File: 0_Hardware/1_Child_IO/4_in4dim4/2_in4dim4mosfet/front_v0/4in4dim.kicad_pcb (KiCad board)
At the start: 2 copper layers, 100.1 x 86.4 mm, 37 parts, among them IC1 ATTINY48-A, P1 CONN_8X2, P2 CONN_2, P3 CONN_2, P4 CONN_2, P5 CONN_2, Q1 PNP, Q2 PNP, Q3 PNP, Q4 PNP

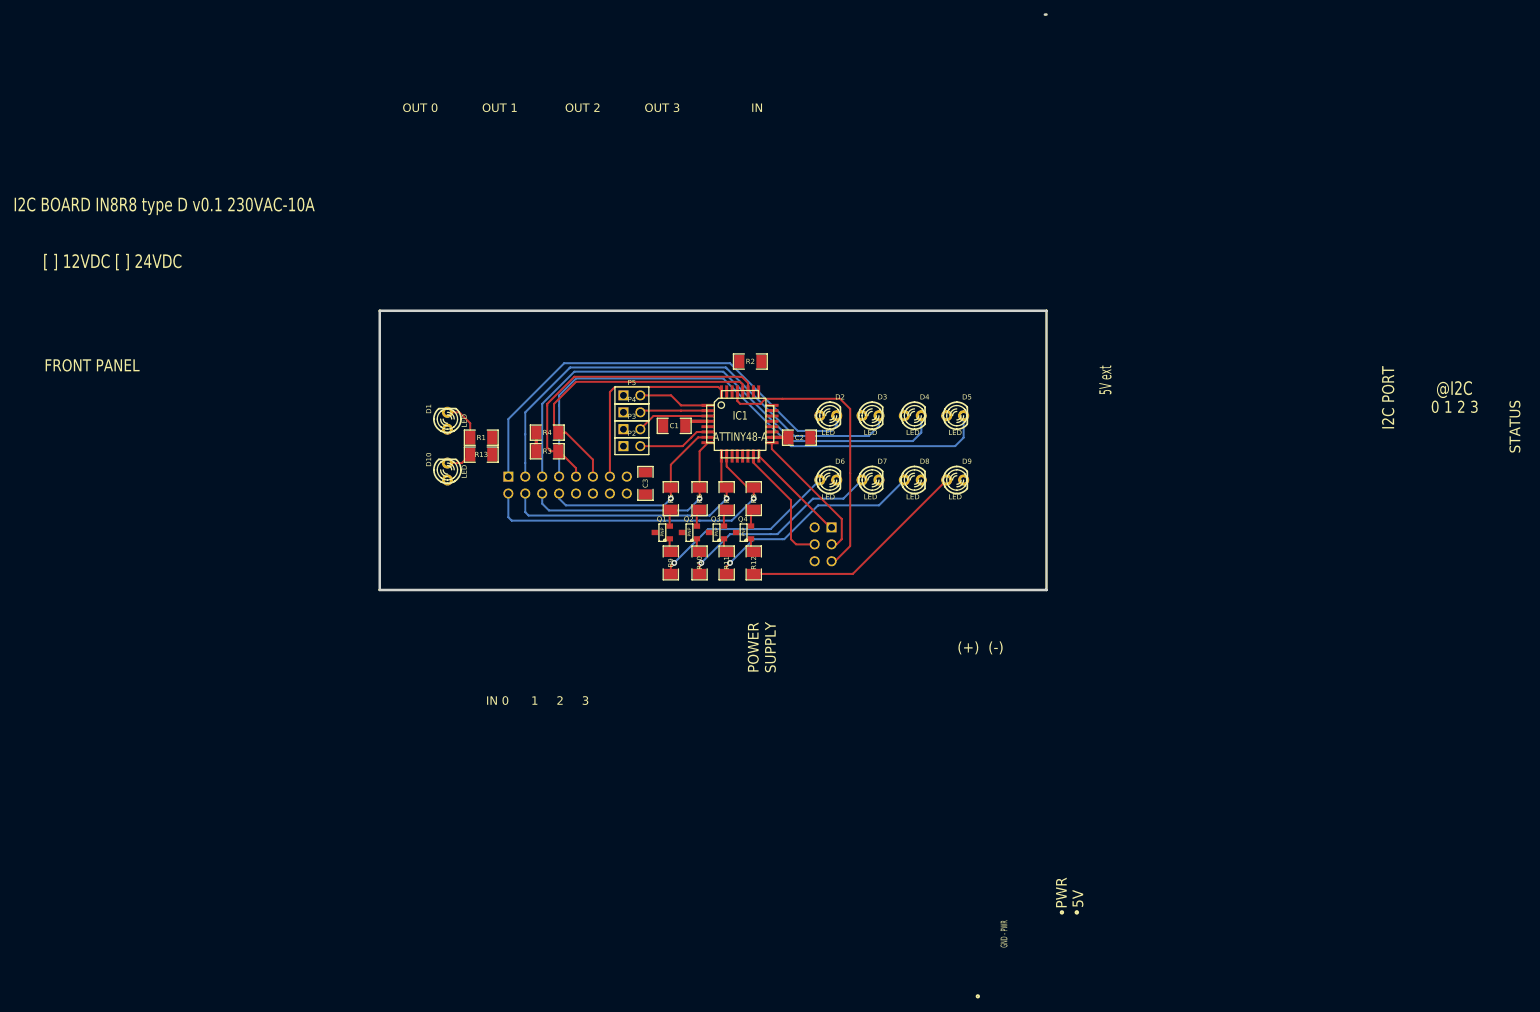
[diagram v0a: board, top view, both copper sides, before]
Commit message: Mise à jour du PCB Front Panel in4dim4mosfet   -> Inversion des broches dans le schéma pour faciliter le routage        * CMD0 Broche7 => Broche 10 de l'attiny        * CMD1 Broche8 => Broche 9 de l'attiny        * CMD2 Broche9 => Broche 8 de l'attiny        * CMD3 Broche10 => Broche 8 de l'attiny   -> Changement des types de led pour D2 à D9 (Transverse en CMS)   -> Mise en place des plan de masse des deux côtés
Mise à jour nom dans les gerber SMB V0.0 pour éviter les pb Smartgit
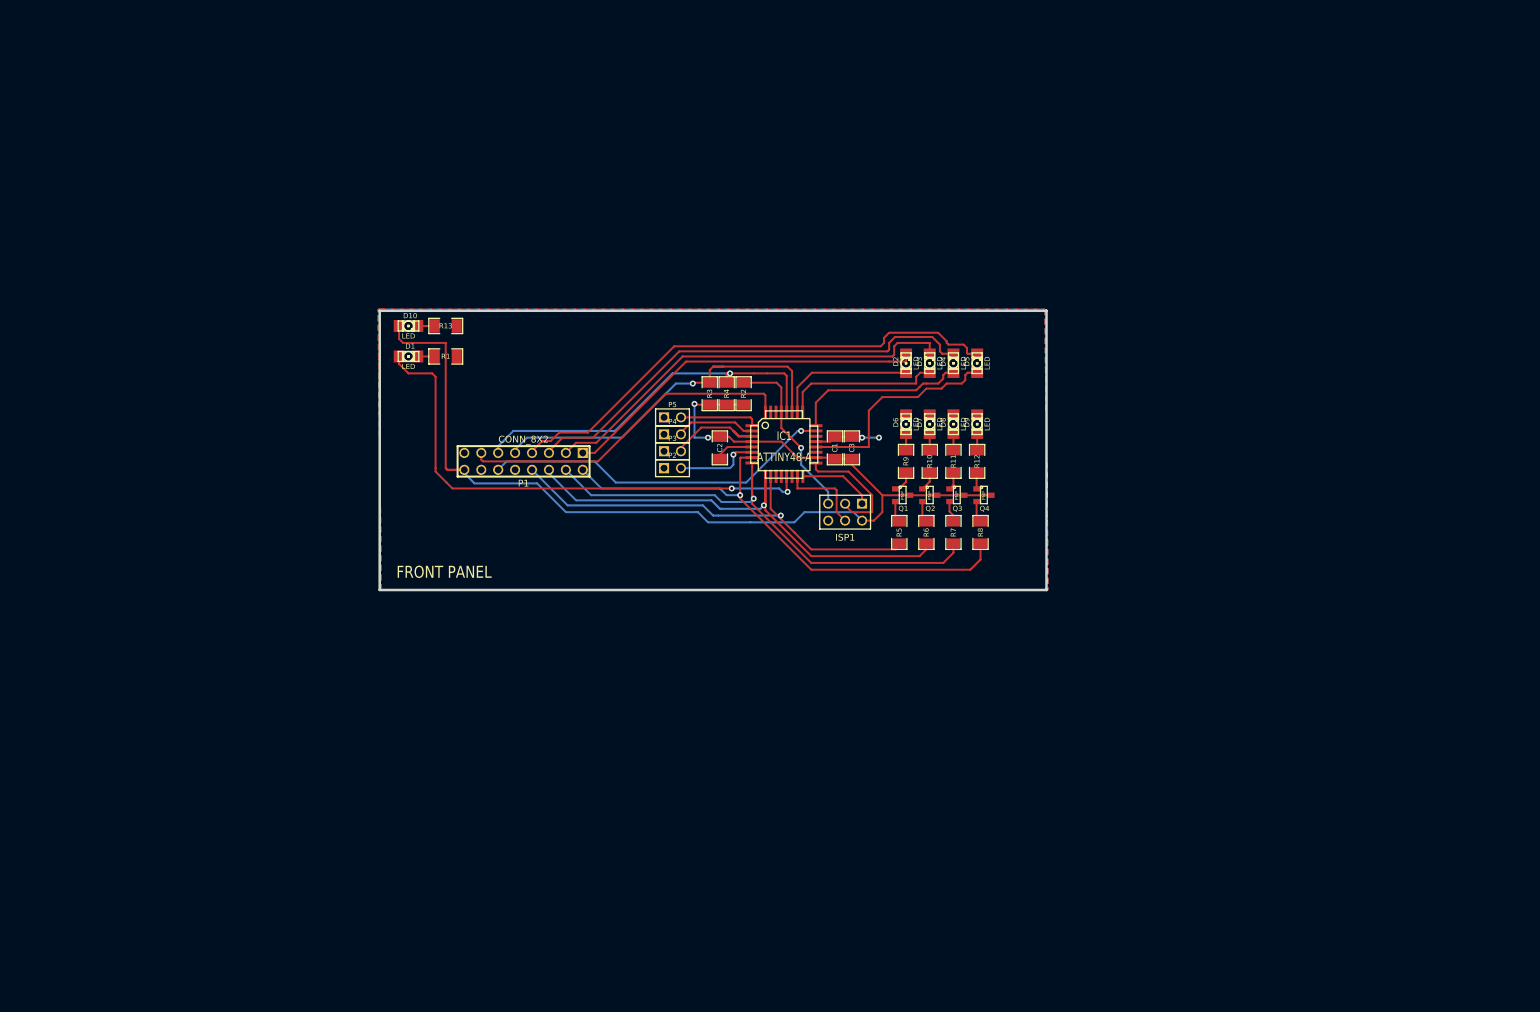
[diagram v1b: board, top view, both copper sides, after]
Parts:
- D1, D10, D2, D3, D4, D5, D6, D7, D8, D9: footprint LED-3MM -> LED-1206
- ISP1, P1: moved to F.Cu
- moved R9 38.5 mm to (260.6, 138.2), turned to 270 degrees
- moved R10 37.8 mm to (264.2, 138.2), turned to 270 degrees
- moved R11 37.3 mm to (267.7, 138.2), turned to 270 degrees
- moved R12 36.8 mm to (271.3, 138.2), turned to 270 degrees
- moved Q1 36.5 mm to (260.1, 143.3), turned to 270 degrees
- moved Q2 36.5 mm to (264.2, 143.3), turned to 270 degrees
- moved Q4 36.5 mm to (272.3, 143.3), turned to 270 degrees
- moved Q3 36.5 mm to (268.2, 143.3), turned to 270 degrees
- moved R5 34.7 mm to (259.6, 148.8), turned to 270 degrees
- moved R7 34.4 mm to (267.7, 148.8), turned to 270 degrees
- moved R6 34.4 mm to (263.7, 148.8), turned to 270 degrees
- moved R8 34.4 mm to (271.8, 148.8), turned to 270 degrees
- moved C3 31.4 mm to (252.5, 136.1)
- moved R4 27.6 mm to (233.7, 128.0), turned to 90 degrees
- moved R3 25.9 mm to (231.1, 128.0), turned to 90 degrees
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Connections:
- IC1 pad 10: CMD3 -> CMD0
- IC1 pad 7: CMD0 -> CMD3
- IC1 pad 8: CMD1 -> CMD2
- IC1 pad 9: CMD2 -> CMD1
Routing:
- net +5V: track 9.02 -> 165.5 mm, vias 0 -> 2
- net LED: track 0.00 -> 78.1 mm, vias 0 -> 2
- net /INT: track 0.00 -> 52.7 mm, vias 0 -> 1
- net CMD1: track 35.2 -> 73.1 mm
- net CMD0: track 30.8 -> 68.0 mm
- net CMD2: track 41.0 -> 76.5 mm
- net _OUT3: track 0.00 -> 32.5 mm
- net N-0000023: track 34.8 -> 2.52 mm
- net N-0000040: track 33.2 -> 2.52 mm, vias 1 -> 0
- net N-0000035: track 31.0 -> 2.52 mm, vias 1 -> 0
- net N-0000036: track 28.9 -> 2.52 mm, vias 1 -> 0
- net _OUT2: track 0.00 -> 26.3 mm
- net CMD3: track 50.6 -> 76.6 mm
- net _OUT1: track 0.00 -> 23.9 mm
- net _OUT0: track 0.00 -> 21.0 mm
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- added copper zone on B.Cu, net GND
- added copper zone on F.Cu, net GND
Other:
- board size 100.1 x 86.4 mm -> 100.1 x 41.9 mm
- board text removed: "(+) (-)"
- board text removed: "0 1 2 3"
- board text removed: "1"
- board text removed: "2"
- board text removed: "3"
- board text removed: "5V"
- board text removed: "5V ext"
- board text removed: "@I2C"
- board text removed: "GND - PWR"
- board text removed: "I2C BOARD IN8R8 type D v0.1 230VAC-10A"
- board text removed: "I2C PORT"
- board text removed: "IN"
- board text removed: "IN 0"
- board text removed: "OUT 0"
- board text removed: "OUT 1"
- board text removed: "OUT 2"
- board text removed: "OUT 3"
- board text removed: "POWER SUPPLY"
- board text removed: "PWR"
- board text removed: "STATUS"
- board text removed: "[ ] 12VDC [ ] 24VDC"

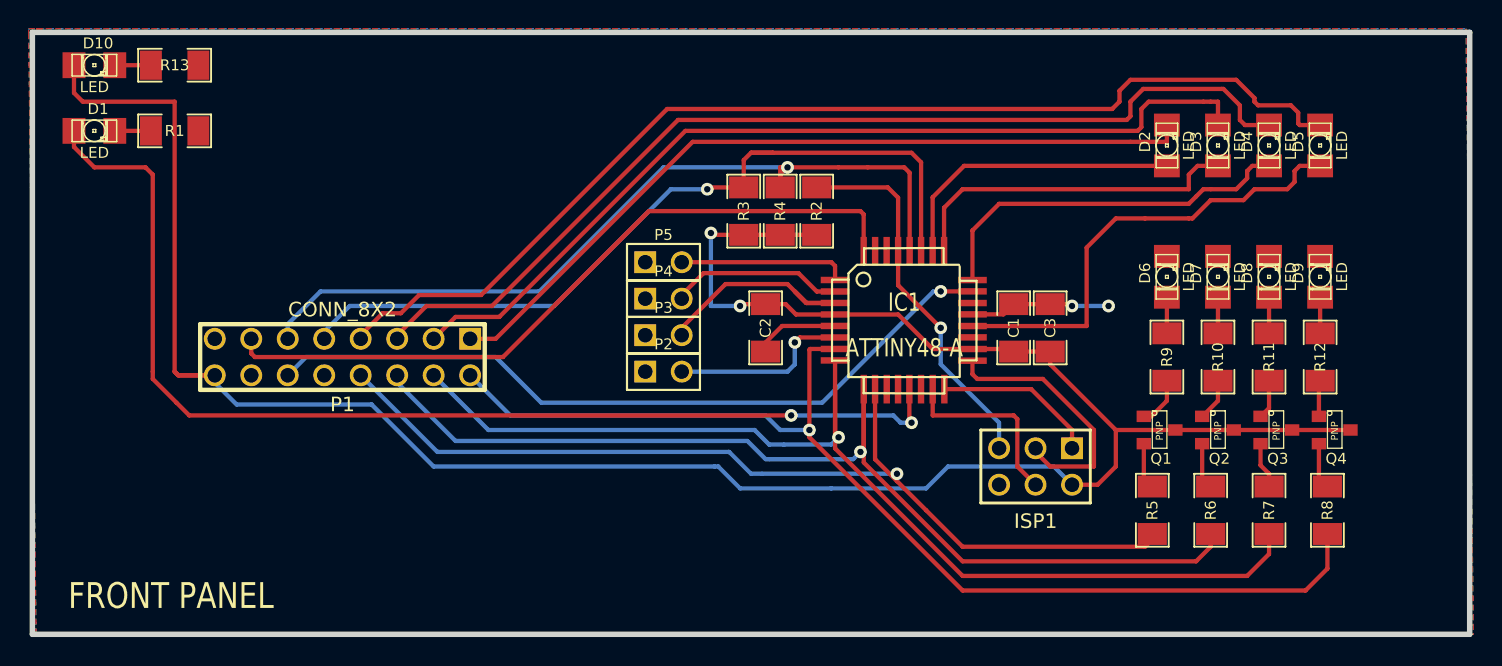
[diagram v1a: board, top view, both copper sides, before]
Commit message: Mise à jour du pcb in4dim4mosfet front :  - Retournerment à 180° du connecteur Back Panel / Front Panel et alignement sur l'axe x avec le connecteur back panel  - Re-routage
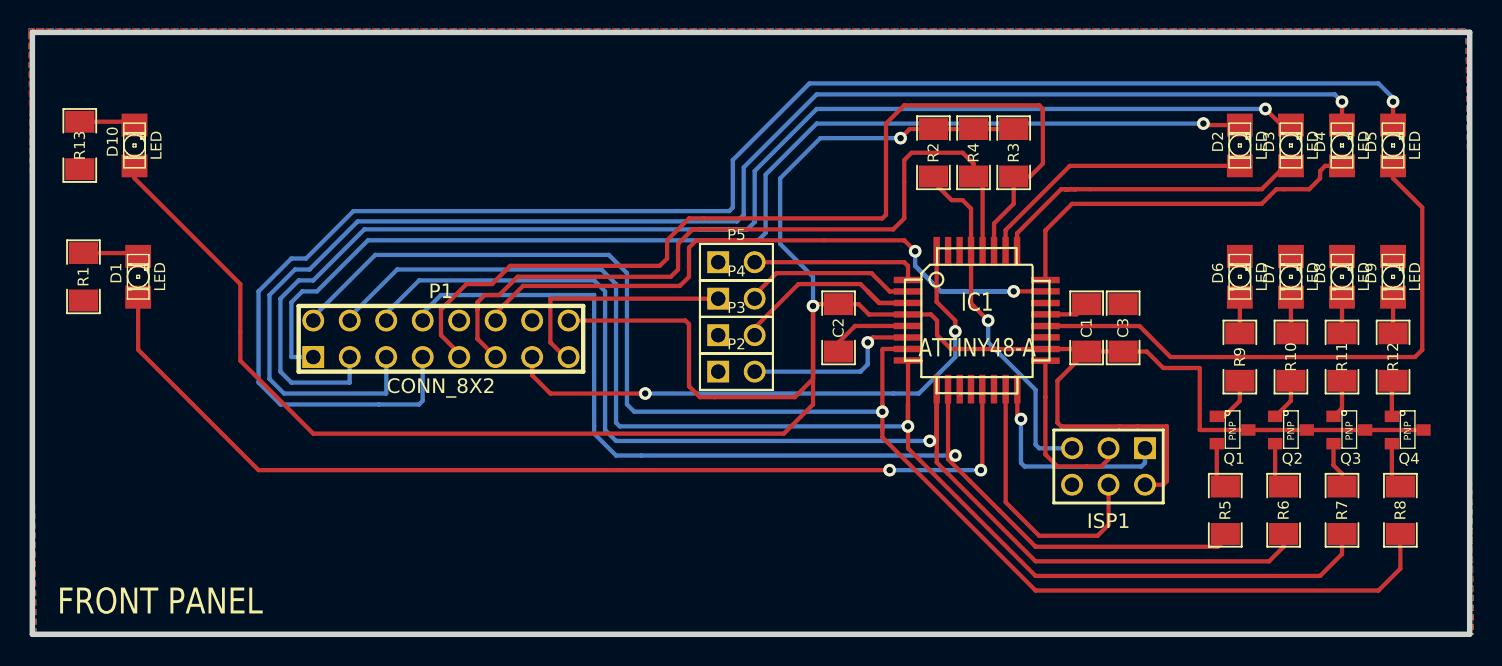
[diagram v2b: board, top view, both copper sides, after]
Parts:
- moved R3 19.2 mm to (249.9, 124.0), turned to 270 degrees
- moved R4 14.1 mm to (247.1, 124.0), turned to 270 degrees
- moved R1 12.0 mm to (185.2, 132.6), turned to 270 degrees
- moved D1 10.6 mm to (189.0, 132.6), turned to 90 degrees
- moved R2 9.09 mm to (244.3, 124.0), turned to 270 degrees
- moved R13 8.65 mm to (184.9, 123.4), turned to 270 degrees
- moved P1 6.97 mm to (210.1, 136.9), turned to 0 degrees
- moved D10 6.25 mm to (188.7, 123.4), turned to 90 degrees
- moved D2 5.08 mm to (265.7, 123.4)
- moved D6 5.08 mm to (265.7, 132.6)
- moved R6 5.08 mm to (268.7, 148.8)
- moved R8 5.08 mm to (276.9, 148.8)
- moved R9 5.08 mm to (265.7, 138.2)
- moved C2 5.08 mm to (237.7, 136.1)
- moved ISP1 5.08 mm to (256.5, 145.8)
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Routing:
- net OUT3: track 76.8 -> 110.8 mm, vias 0 -> 1
- net OUT2: track 70.3 -> 101.2 mm, vias 0 -> 1
- net CMD3: track 76.6 -> 103.5 mm
- net OUT1: track 63.8 -> 90.4 mm, vias 0 -> 1
- net +5V: track 165.5 -> 189.4 mm
- net OUT0: track 55.4 -> 79.0 mm, vias 0 -> 1
- net CMD2: track 76.5 -> 94.3 mm
- net CMD1: track 73.1 -> 87.1 mm
- net SDA: track 56.3 -> 68.9 mm, vias 1 -> 0
- net ZC: track 50.6 -> 40.2 mm, vias 0 -> 2
- net GND: track 15.8 -> 25.5 mm, vias 2 -> 0
- net _OUT3: track 32.5 -> 41.0 mm
- net CMD0: track 68.0 -> 76.2 mm
- net LED: track 78.1 -> 71.5 mm
- net MOSI: track 12.9 -> 19.1 mm
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
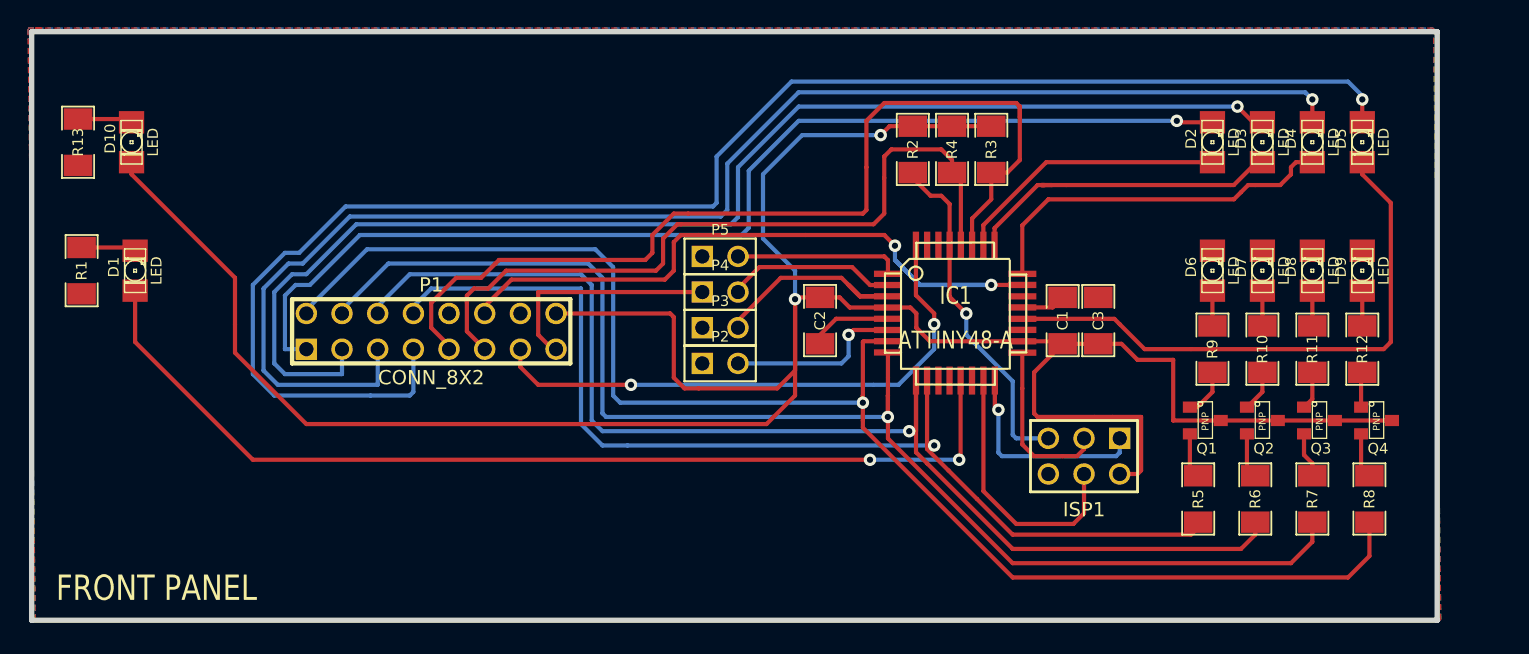
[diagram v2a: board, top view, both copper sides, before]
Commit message: Mise à jour du Front Panel in4dim4 mosfet
- Ecartement des composants
- Inversion des broches de sorties de l'attinye OUT0 à 4 pour faciliter le routage
- Ajout de la sérigraphie
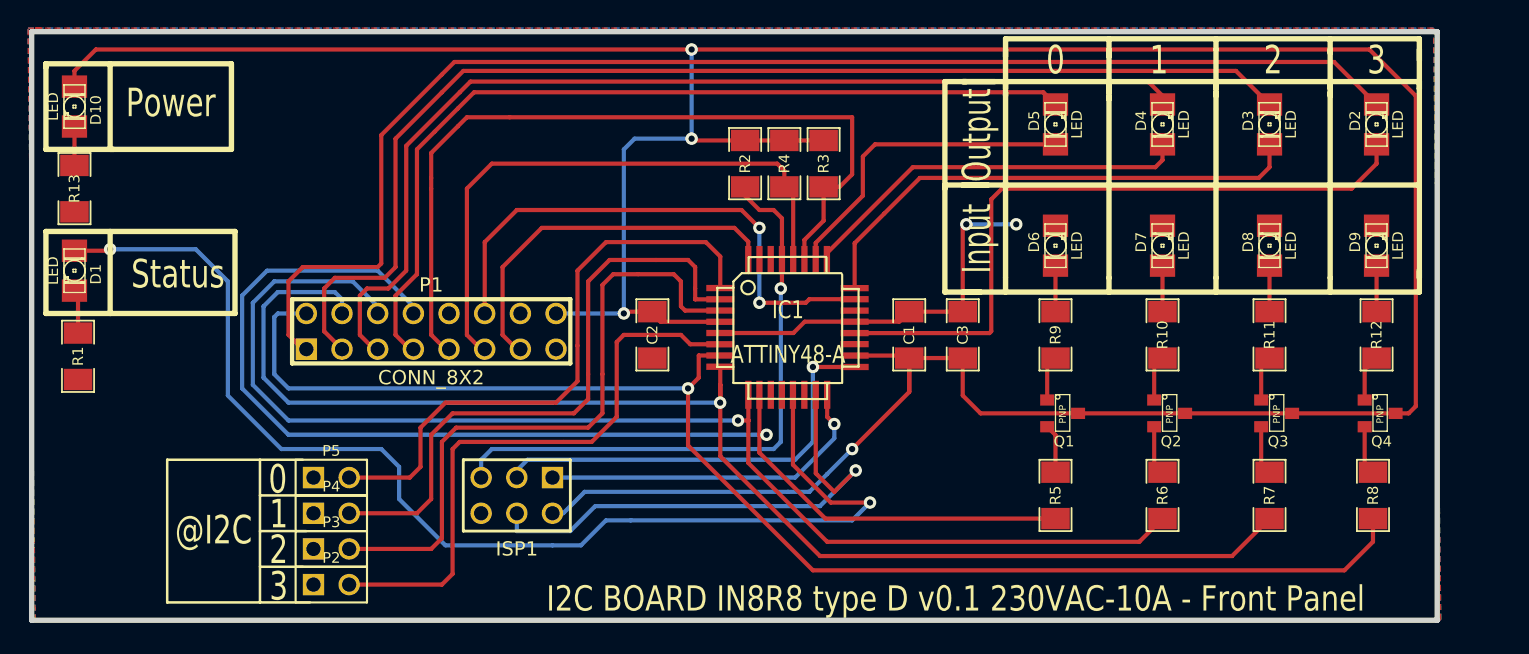
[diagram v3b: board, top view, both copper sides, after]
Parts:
- moved ISP1 40.5 mm to (216.2, 148.6)
- moved P3 31.9 mm to (202.9, 152.4)
- moved P4 31.9 mm to (202.9, 149.9)
- moved P2 31.9 mm to (202.9, 154.9)
- moved P5 31.9 mm to (202.9, 147.3)
- moved D5 21.9 mm to (254.5, 122.2)
- moved R2 12.0 mm to (232.4, 125.0)
- moved R3 12.0 mm to (238.0, 125.0)
- moved C2 12.0 mm to (225.8, 137.2)
- moved IC1 12.0 mm to (235.5, 136.7)
- moved R4 12.0 mm to (235.2, 125.0)
- moved D2 11.8 mm to (277.4, 122.2)
- moved D6 11.3 mm to (254.5, 130.8)
- moved R9 11.2 mm to (254.5, 137.2)
- moved C1 11.0 mm to (244.1, 137.2)
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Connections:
- IC1 pad 20: _OUT3 -> _OUT0
- IC1 pad 24: _OUT2 -> _OUT1
- IC1 pad 25: _OUT1 -> _OUT2
- IC1 pad 26: _OUT0 -> _OUT3
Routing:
- net +5V: track 189.4 -> 242.7 mm, vias 2 -> 4
- net OUT3: track 110.8 -> 63.0 mm, vias 1 -> 0
- net A1: track 12.1 -> 44.0 mm
- net A0: track 11.8 -> 42.3 mm
- net A3: track 12.6 -> 42.4 mm, vias 1 -> 0
- net _OUT0: track 19.6 -> 49.0 mm
- net A2: track 17.3 -> 46.0 mm
- net OUT2: track 101.2 -> 74.2 mm, vias 1 -> 0
- net SCK: track 12.2 -> 30.7 mm, vias 0 -> 1
- net RESET: track 24.7 -> 43.0 mm
- net _OUT3: track 41.0 -> 22.8 mm
- net MOSI: track 19.1 -> 36.8 mm, vias 0 -> 1
- net OUT0: track 79.0 -> 96.1 mm, vias 1 -> 0
- net /INT: track 51.7 -> 38.3 mm
- net ZC: track 40.2 -> 26.9 mm, vias 2 -> 0
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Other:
- board text added: "0"
- board text added: "1"
- board text added: "2"
- board text added: "3"
- board text added: "@I2C"
- board text added: "I2C BOARD IN8R8 type D v0.1 230VAC-10A - Front Panel"
- board text added: "Input"
- board text added: "Output"
- board text added: "Power"
- board text added: "Status"
- board text removed: "FRONT PANEL"
